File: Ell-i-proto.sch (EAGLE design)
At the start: 148 parts, among them J1 TSM-106-01-L-SH, J10 KLDX-SMT2-0202, J2 PWMH, J3 PWR, J4 PWML, J5 ANAL, J6 SPI, J7 COMM, J8 ANAH, J9 RJ45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

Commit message: Changed 1x6 pinstrip to an FTDI-connector component.
Changed middle layer wires with outer layer wires:

- Under T1
- Left of U6

Optimized away vias for J2 and J4 pins.

Other optimizations.
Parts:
- removed J1: TSM-106-01-L-SH, ell-i:TSM-106-01-L-SH
- added U$4: FTDI-SER-6-HOR2, ell-i:FTDI-SER-6-HOR2
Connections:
- net GNDI: now also U$4.GND; no longer J1.6
- net N$6: now also U$4.-CTS; no longer J1.5
- net NDSR2: now also U$4.-RTS; no longer J1.1
- net RX2: now also U$4.TXD; no longer J1.3
- net TX2: now also U$4.RXD; no longer J1.2
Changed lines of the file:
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@@
 <part name="FID3" library="ell-i" deviceset="MOUNT_FIDUCIAL" device=""/>
 <part name="Y1" library="crystal" deviceset="CRYSTAL" device="SM49"/>
-<part name="J1" library="ell-i" deviceset="TSM-106-01-L-SH" device=""/>
 <part name="C45" library="ell-i" deviceset="C" device="0805" value="22u"/>
 <part name="C34" library="ell-i" deviceset="C" device="0805" value="22u"/>
@@
 <part name="C48" library="ell-i" deviceset="C" device="0805" value="22u"/>
 <part name="PE2" library="supply1" deviceset="PE" device=""/>
+<part name="U$4" library="ell-i" deviceset="FTDI-SER-6" device="-HOR2"/>
 </parts>
 <sheets>
@@
 <instance part="S1" gate="G$1" x="38.1" y="114.3" rot="R270"/>
 <instance part="Y1" gate="G$1" x="63.5" y="76.2"/>
-<instance part="J1" gate="G$1" x="15.24" y="142.24" rot="R180"/>
+<instance part="U$4" gate="G$1" x="15.24" y="139.7" rot="MR180"/>
 </instances>
 <busses>
@@
 <pinref part="D3" gate="G$1" pin="C"/>
 <wire x1="25.4" y1="68.58" x2="25.4" y2="134.62" width="0.1524" layer="91"/>
-<wire x1="25.4" y1="134.62" x2="17.78" y2="134.62" width="0.1524" layer="91"/>
-<pinref part="J1" gate="G$1" pin="1"/>
+<wire x1="25.4" y1="134.62" x2="22.86" y2="134.62" width="0.1524" layer="91"/>
+<pinref part="U$4" gate="G$1" pin="-RTS"/>
 </segment>
 </net>
@@
 </segment>
 <segment>
-<wire x1="27.94" y1="139.7" x2="17.78" y2="139.7" width="0.1524" layer="91"/>
+<wire x1="27.94" y1="139.7" x2="22.86" y2="139.7" width="0.1524" layer="91"/>
 <label x="27.94" y="139.7" size="1.016" layer="95" xref="yes"/>
-<pinref part="J1" gate="G$1" pin="3"/>
+<pinref part="U$4" gate="G$1" pin="TXD"/>
 </segment>
 </net>
@@
 <segment>
 <label x="27.94" y="137.16" size="1.016" layer="95" xref="yes"/>
-<wire x1="17.78" y1="137.16" x2="27.94" y2="137.16" width="0.1524" layer="91"/>
-<pinref part="J1" gate="G$1" pin="2"/>
+<pinref part="U$4" gate="G$1" pin="RXD"/>
+<wire x1="22.86" y1="137.16" x2="27.94" y2="137.16" width="0.1524" layer="91"/>
 </segment>
 </net>
@@
 <segment>
 <pinref part="GNDI21" gate="G$1" pin="GNDI"/>
-<wire x1="17.78" y1="147.32" x2="55.88" y2="147.32" width="0.1524" layer="91"/>
-<pinref part="J1" gate="G$1" pin="6"/>
+<pinref part="U$4" gate="G$1" pin="GND"/>
+<wire x1="22.86" y1="147.32" x2="55.88" y2="147.32" width="0.1524" layer="91"/>
 </segment>
 <segment>
@@
 <pinref part="D1" gate="G$1" pin="C"/>
 <wire x1="50.8" y1="134.62" x2="50.8" y2="144.78" width="0.1524" layer="91"/>
-<wire x1="50.8" y1="144.78" x2="17.78" y2="144.78" width="0.1524" layer="91"/>
-<pinref part="J1" gate="G$1" pin="5"/>
-</segment>
-</net>
+<wire x1="50.8" y1="144.78" x2="22.86" y2="144.78" width="0.1524" layer="91"/>
+<pinref part="U$4" gate="G$1" pin="-CTS"/>
+</segment>
+</net>

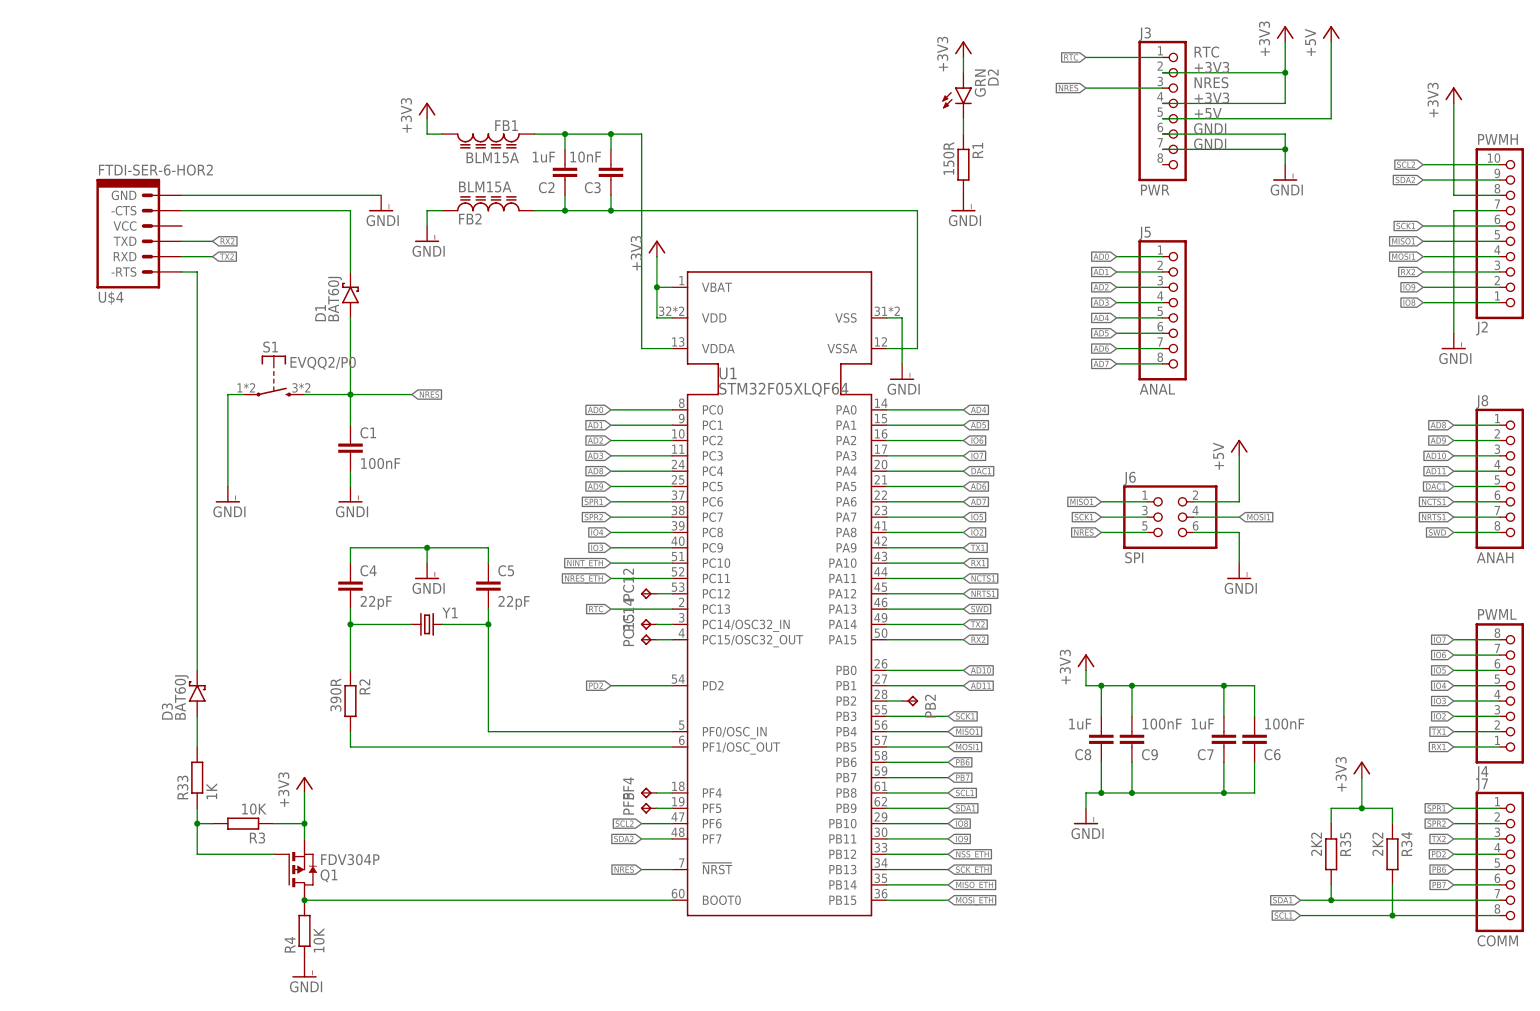
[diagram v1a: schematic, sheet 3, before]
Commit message: Comments and limitations from PV and PNR applied, generic clearances increased to 0.2mm
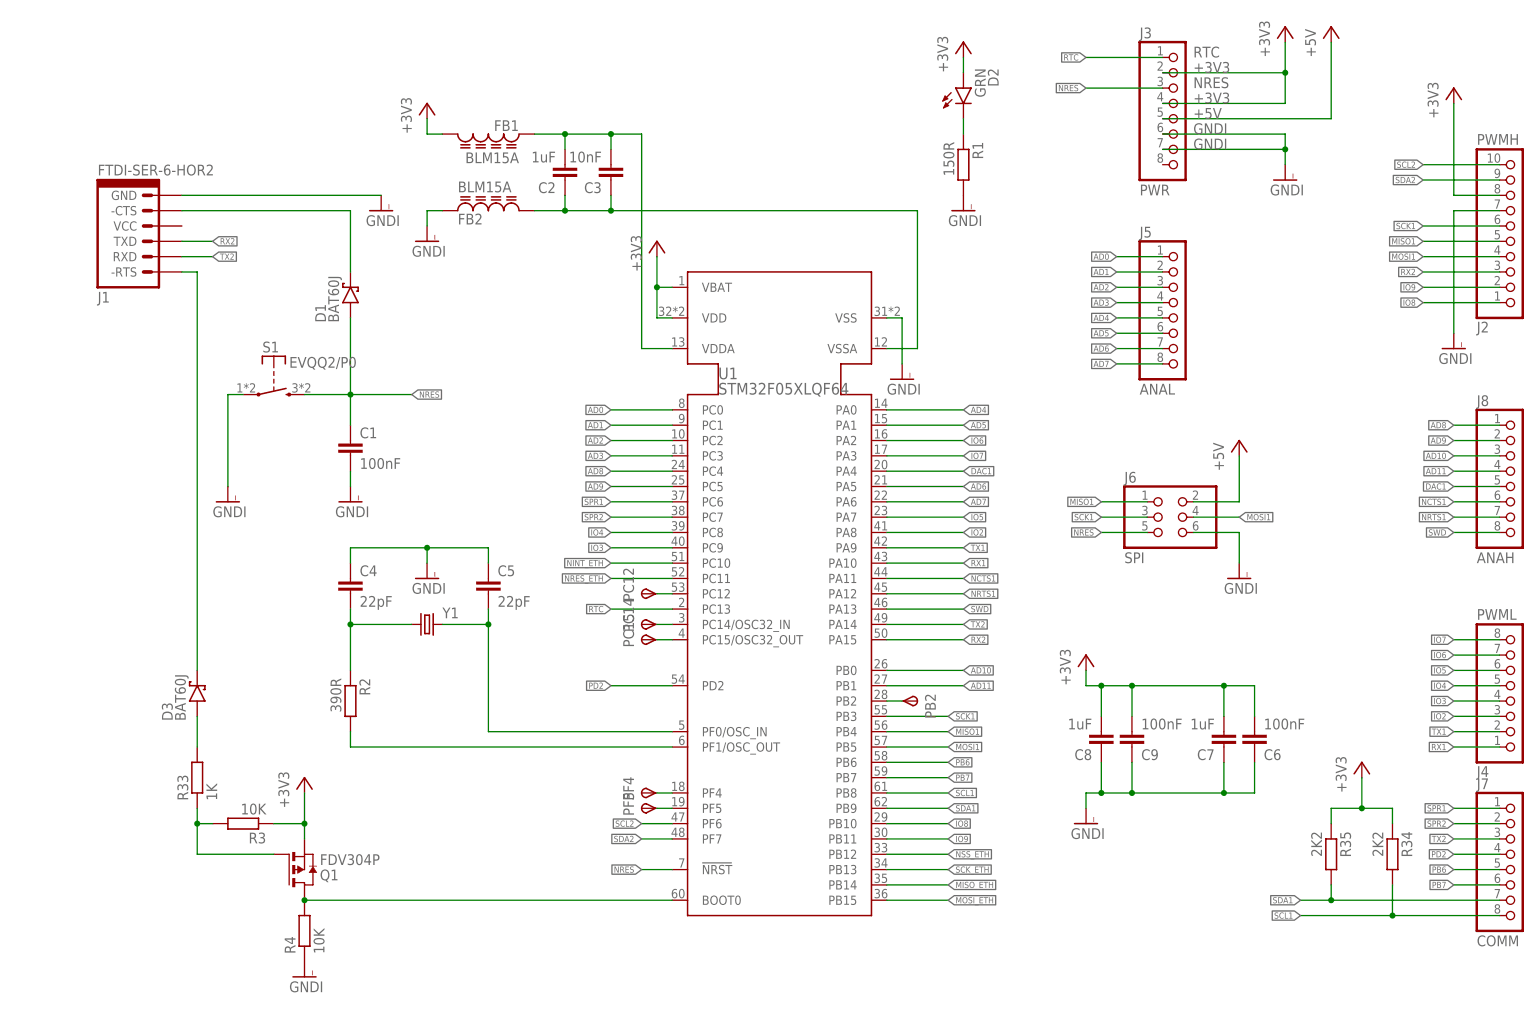
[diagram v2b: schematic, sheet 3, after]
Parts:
- C29, C30: device rcl:C-EUC1210 -> ell-i:C0805
- PB2, PC12, PC14, PC15, PF4, PF5: value TPTP06R -> TPSB1,27; device testpad:TPTP06R -> testpad:TPSB1,27
- renumbered U$4 to J1
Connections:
- net N$2: now also PC14.PP; no longer PC14.TP
- net N$3: now also PC15.PP; no longer PC15.TP
- net N$5: now also PF4.PP; no longer PF4.TP
- net N$7: now also PF5.PP; no longer PF5.TP
- net N$8: now also PB2.PP; no longer PB2.TP
- net N$9: now also PC12.PP; no longer PC12.TP
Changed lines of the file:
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@@
 <part name="C27" library="ell-i" deviceset="C" device="0402" value="22pF"/>
 <part name="C28" library="ell-i" deviceset="C" device="0402" value="22pF"/>
-<part name="C29" library="rcl" deviceset="C-EU" device="C1210" value="68pF"/>
-<part name="C30" library="rcl" deviceset="C-EU" device="C1210" value="1uF"/>
+<part name="C29" library="ell-i" deviceset="C" device="0805" value="68pF"/>
+<part name="C30" library="ell-i" deviceset="C" device="0805" value="1uF"/>
 <part name="C32" library="ell-i" deviceset="C" device="0402" value="100nF"/>
 <part name="C33" library="rcl" deviceset="CPOL-US" device="CT3216" value="opt tant"/>
@@
 <part name="+3V11" library="supply1" deviceset="+3V3" device=""/>
 <part name="GNDI24" library="supply1" deviceset="GNDI" device=""/>
-<part name="PC14" library="testpad" deviceset="TP" device="TP06R"/>
-<part name="PC15" library="testpad" deviceset="TP" device="TP06R"/>
-<part name="PF4" library="testpad" deviceset="TP" device="TP06R"/>
-<part name="PF5" library="testpad" deviceset="TP" device="TP06R"/>
-<part name="PB2" library="testpad" deviceset="TP" device="TP06R"/>
-<part name="PC12" library="testpad" deviceset="TP" device="TP06R"/>
+<part name="PC14" library="testpad" deviceset="TPS" device="B1,27"/>
+<part name="PC15" library="testpad" deviceset="TPS" device="B1,27"/>
+<part name="PF4" library="testpad" deviceset="TPS" device="B1,27"/>
+<part name="PF5" library="testpad" deviceset="TPS" device="B1,27"/>
+<part name="PB2" library="testpad" deviceset="TPS" device="B1,27"/>
+<part name="PC12" library="testpad" deviceset="TPS" device="B1,27"/>
 <part name="+3V12" library="supply1" deviceset="+3V3" device=""/>
 <part name="GNDI7" library="supply1" deviceset="GNDI" device=""/>
@@
 <part name="C48" library="ell-i" deviceset="C" device="0805" value="22u"/>
 <part name="PE2" library="supply1" deviceset="PE" device=""/>
-<part name="U$4" library="ell-i" deviceset="FTDI-SER-6" device="-HOR2"/>
+<part name="J1" library="ell-i" deviceset="FTDI-SER-6" device="-HOR2"/>
 </parts>
 <sheets>
@@
 </segment>
 </net>
-<net name="N27571" class="1">
+<net name="N27571" class="2">
 <segment>
 <pinref part="C29" gate="G$1" pin="1"/>
@@
 </segment>
 </net>
-<net name="N27735" class="1">
+<net name="N27735" class="2">
 <segment>
 <pinref part="R24" gate="G$1" pin="1"/>
@@
 <instance part="S1" gate="G$1" x="38.1" y="114.3" rot="R270"/>
 <instance part="Y1" gate="G$1" x="63.5" y="76.2"/>
-<instance part="U$4" gate="G$1" x="15.24" y="139.7" rot="MR180"/>
+<instance part="J1" gate="G$1" x="15.24" y="139.7" rot="MR180"/>
 </instances>
 <busses>
@@
 <wire x1="25.4" y1="68.58" x2="25.4" y2="134.62" width="0.1524" layer="91"/>
 <wire x1="25.4" y1="134.62" x2="22.86" y2="134.62" width="0.1524" layer="91"/>
-<pinref part="U$4" gate="G$1" pin="-RTS"/>
+<pinref part="J1" gate="G$1" pin="-RTS"/>
 </segment>
 </net>
@@
 <wire x1="27.94" y1="139.7" x2="22.86" y2="139.7" width="0.1524" layer="91"/>
 <label x="27.94" y="139.7" size="1.016" layer="95" xref="yes"/>
-<pinref part="U$4" gate="G$1" pin="TXD"/>
+<pinref part="J1" gate="G$1" pin="TXD"/>
 </segment>
 </net>
@@
 <segment>
 <label x="27.94" y="137.16" size="1.016" layer="95" xref="yes"/>
-<pinref part="U$4" gate="G$1" pin="RXD"/>
+<pinref part="J1" gate="G$1" pin="RXD"/>
 <wire x1="22.86" y1="137.16" x2="27.94" y2="137.16" width="0.1524" layer="91"/>
 </segment>
@@
 <segment>
 <pinref part="GNDI21" gate="G$1" pin="GNDI"/>
-<pinref part="U$4" gate="G$1" pin="GND"/>
+<pinref part="J1" gate="G$1" pin="GND"/>
 <wire x1="22.86" y1="147.32" x2="55.88" y2="147.32" width="0.1524" layer="91"/>
 </segment>
@@
 <wire x1="50.8" y1="134.62" x2="50.8" y2="144.78" width="0.1524" layer="91"/>
 <wire x1="50.8" y1="144.78" x2="22.86" y2="144.78" width="0.1524" layer="91"/>
-<pinref part="U$4" gate="G$1" pin="-CTS"/>
+<pinref part="J1" gate="G$1" pin="-CTS"/>
 </segment>
 </net>
@@
 <net name="N$2" class="0">
 <segment>
-<pinref part="PC14" gate="G$1" pin="TP"/>
+<pinref part="PC14" gate="G$1" pin="PP"/>
 <pinref part="U1" gate="G$1" pin="PC14/OSC32_IN"/>
 <wire x1="101.6" y1="76.2" x2="104.14" y2="76.2" width="0.1524" layer="91"/>
@@
 <net name="N$3" class="0">
 <segment>
-<pinref part="PC15" gate="G$1" pin="TP"/>
+<pinref part="PC15" gate="G$1" pin="PP"/>
 <pinref part="U1" gate="G$1" pin="PC15/OSC32_OUT"/>
 <wire x1="101.6" y1="73.66" x2="104.14" y2="73.66" width="0.1524" layer="91"/>
@@
 <net name="N$5" class="0">
 <segment>
-<pinref part="PF4" gate="G$1" pin="TP"/>
+<pinref part="PF4" gate="G$1" pin="PP"/>
 <pinref part="U1" gate="G$1" pin="PF4"/>
 <wire x1="101.6" y1="48.26" x2="104.14" y2="48.26" width="0.1524" layer="91"/>
@@
 <net name="N$7" class="0">
 <segment>
-<pinref part="PF5" gate="G$1" pin="TP"/>
+<pinref part="PF5" gate="G$1" pin="PP"/>
 <pinref part="U1" gate="G$1" pin="PF5"/>
 <wire x1="101.6" y1="45.72" x2="104.14" y2="45.72" width="0.1524" layer="91"/>
@@
 <segment>
 <pinref part="U1" gate="G$1" pin="PB2"/>
-<pinref part="PB2" gate="G$1" pin="TP"/>
+<pinref part="PB2" gate="G$1" pin="PP"/>
 <wire x1="139.7" y1="63.5" x2="142.24" y2="63.5" width="0.1524" layer="91"/>
 </segment>
@@
 <net name="N$9" class="0">
 <segment>
-<pinref part="PC12" gate="G$1" pin="TP"/>
+<pinref part="PC12" gate="G$1" pin="PP"/>
 <pinref part="U1" gate="G$1" pin="PC12"/>
 <wire x1="101.6" y1="81.28" x2="104.14" y2="81.28" width="0.1524" layer="91"/>
